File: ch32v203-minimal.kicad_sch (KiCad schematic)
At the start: 21 parts, among them J1 Conn_01x08, J3 Conn_01x04, J4 Conn_01x04, J5 Conn_02x10_Odd_Even, SW1 SW_Push, SW2 SW_Push, U1 AMS1117-3.3, U2 CH32V203K8T6, Y1 8MHz

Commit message: Rework layout
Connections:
- net NRST: now reaches C9.1, SW2.2, U2.4 (NRST)
- net BOOT0: now reaches R1.1, SW1.2, U2.31 (BOOT0/PB8)
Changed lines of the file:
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@@
+		)
+	)
+	(label "NRST"
+		(at 92.71 88.9 0)
+		(effects
+			(font
+				(size 1.27 1.27)
+			)
+			(justify left bottom)
 		)
 	)
@@
 		(effects
 			(font
+				(size 1.27 1.27)
+			)
+			(justify left bottom)
+		)
+	)
+	(label "BOOT0"
+		(at 210.82 78.74 0)
+		(effects
+			(font

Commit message: Add +5V connector
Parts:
- added J2: Conn_01x02_Pin, Connector_PinHeader_2.54mm:PinHeader_1x02_P2.54mm_Vertical, symbol Connector:Conn_01x02_Pin
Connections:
- net +5V: now also J2.1 (Pin_1)
- net GND: now also J2.2 (Pin_2)
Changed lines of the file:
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@@
 	)
 	(junction
+		(at 59.69 49.53)
+		(diameter 0)
+		(color 0 0 0 0)
+	)
+	(junction
 		(at 168.91 35.56)
 		(diameter 0)
@@
 	(wire
 		(pts
+			(xy 59.69 49.53) (xy 59.69 90.17)
+		)
+		(stroke
+			(width 0)
+			(type default)
+		)
+	)
+	(wire
+		(pts
 			(xy 88.9 76.2) (xy 93.98 76.2)
 		)
@@
 	(wire
 		(pts
-			(xy 59.69 25.4) (xy 59.69 90.17)
+			(xy 59.69 25.4) (xy 59.69 49.53)
 		)
 		(stroke
@@
 	(wire
 		(pts
+			(xy 52.07 49.53) (xy 59.69 49.53)
+		)
+		(stroke
+			(width 0)
+			(type default)
+		)
+	)
+	(wire
+		(pts
 			(xy 219.71 93.98) (xy 219.71 96.52)
 		)
@@
 	(wire
 		(pts
+			(xy 52.07 54.61) (xy 52.07 52.07)
+		)
+		(stroke
+			(width 0)
+			(type default)
+		)
+	)
+	(wire
+		(pts
 			(xy 182.88 39.37) (xy 195.58 39.37)
 		)
@@
 	)
 	(symbol
+		(lib_id "power:GND")
+		(at 52.07 54.61 0)
+		(mirror y)
+		(unit 1)
+		(body_style 1)
+		(exclude_from_sim no)
+		(in_bom yes)
+		(on_board yes)
+		(in_pos_files yes)
+		(dnp no)
+		(fields_autoplaced yes)
+		(property "Reference" "#PWR023"
+			(at 52.07 60.96 0)
+			(hide yes)
+			(show_name no)
+			(do_not_autoplace no)
+			(effects
+				(font
+					(size 1.27 1.27)
+				)
+			)
+		)
+		(property "Value" "GND"
+			(at 52.07 59.69 0)
+			(show_name no)
+			(do_not_autoplace no)
+			(effects
+				(font
+					(size 1.27 1.27)
+				)
+			)
+		)
+		(property "Footprint" ""
+			(at 52.07 54.61 0)
+			(hide yes)
+			(show_name no)
+			(do_not_autoplace no)
+			(effects
+				(font
+					(size 1.27 1.27)
+				)
+			)
+		)
+		(property "Datasheet" ""
+			(at 52.07 54.61 0)
+			(hide yes)
+			(show_name no)
+			(do_not_autoplace no)
+			(effects
+				(font
+					(size 1.27 1.27)
+				)
+			)
+		)
+		(property "Description" "Power symbol creates a global label with name \"GND\" , ground"
+			(at 52.07 54.61 0)
+			(hide yes)
+			(show_name no)
+			(do_not_autoplace no)
+			(effects
+				(font
+					(size 1.27 1.27)
+				)
+			)
+		)
+		(pin "1"
+		)
+		(instances
+			(project "ch32v203-minimal"
+				(path "/c4c3c12b-dd2c-4da1-bb89-311f762bf82a"
+					(reference "#PWR023")
+					(unit 1)
+				)
+			)
+		)
+	)
+	(symbol
 		(lib_id "Device:C")
 		(at 153.67 44.45 0)
@@
 					(unit 1)
 				)
+			)
+		)
+	)
+	(symbol
+		(lib_id "Connector:Conn_01x02_Pin")
+		(at 46.99 49.53 0)
+		(unit 1)
+		(body_style 1)
+		(exclude_from_sim no)
+		(in_bom yes)
+		(on_board yes)
+		(in_pos_files yes)
+		(dnp no)
+		(fields_autoplaced yes)
+		(property "Reference" "J2"
+			(at 47.625 44.45 0)
+			(show_name no)
+			(do_not_autoplace no)
+			(effects
+				(font
+					(size 1.27 1.27)
+				)
+			)
+		)
+		(property "Value" "Conn_01x02_Pin"
+			(at 47.625 46.99 0)
+			(show_name no)
+			(do_not_autoplace no)
+			(effects
+				(font
+					(size 1.27 1.27)
+				)
+			)
+		)
+		(property "Footprint" "Connector_PinHeader_2.54mm:PinHeader_1x02_P2.54mm_Vertical"
+			(at 46.99 49.53 0)
+			(hide yes)
+			(show_name no)
+			(do_not_autoplace no)
+			(effects
+				(font
+					(size 1.27 1.27)
+				)
+			)
+		)
+		(property "Datasheet" ""
+			(at 46.99 49.53 0)
+			(hide yes)
+			(show_name no)
+			(do_not_autoplace no)
+			(effects
+				(font
+					(size 1.27 1.27)
+				)
+			)
+		)
+		(property "Description" "Generic connector, single row, 01x02, script generated"
+			(at 46.99 49.53 0)
+			(hide yes)
+			(show_name no)
+			(do_not_autoplace no)
+			(effects
+				(font
+					(size 1.27 1.27)
+				)
+			)
+		)
+		(pin "1"
+		)
+		(pin "2"
+		)
+		(instances
+			(project "ch32v203-minimal"
+				(path "/c4c3c12b-dd2c-4da1-bb89-311f762bf82a"
+					(reference "J2")
+					(unit 1)
+				)

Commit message: Add proto board
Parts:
- added D2: SS14, Diode_SMD:D_SMA, symbol Diode:SS14
- added H1, H2, H3, H4, H5: MountingHole_Pad, MountingHole:MountingHole_2.2mm_M2_DIN965_Pad, symbol Mechanical:MountingHole_Pad
- added TP1, TP2: TestPoint, 0_Local:Proto-1x16, symbol Connector:TestPoint
- added TP10, TP11, TP12, TP13, TP14, TP15, TP16, TP17, TP18, TP3, TP4, TP5, TP6, TP7, TP8, TP9: TestPoint, 0_Local:Proto-1x4, symbol Connector:TestPoint
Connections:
- net +3V3: now also TP2.1
- net +5V: now also D2.2 (A); no longer C1.1, J2.1 (Pin_1), U1.3 (VI)
- net GND: now also H1.1, H2.1, H3.1, H4.1, H5.1, TP1.1
- new net Row 1: TP3.1
- new net Row 10: TP12.1
- new net Row 11: TP13.1
- new net Row 12: TP14.1
- new net Row 13: TP15.1
- new net Row 14: TP16.1
- new net Row 15: TP17.1
- new net Row 16: TP18.1
- new net Row 2: TP4.1
- new net Row 3: TP5.1
- new net Row 4: TP6.1
- new net Row 5: TP7.1
- new net Row 6: TP8.1
- new net Row 7: TP9.1
- new net Row 8: TP10.1
- new net Row 9: TP11.1
- new net VBUS: C1.1, D2.1 (K), J2.1 (Pin_1), U1.3 (VI)
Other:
- note added: "Proto Area"
- moved on the sheet: C1, C2, C3, C4, C5, C6, C7, C8, C9, D1, J1, J2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

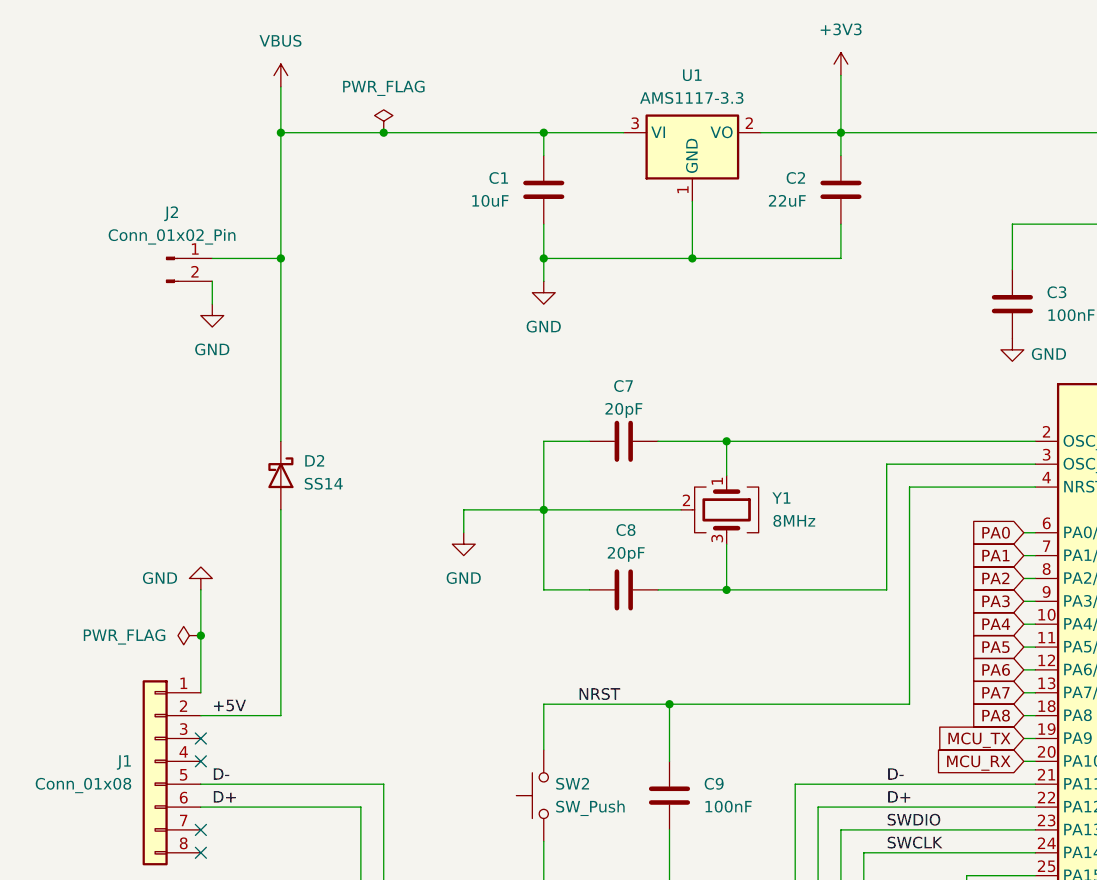
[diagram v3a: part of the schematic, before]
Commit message: Swap LDO for MCP1700
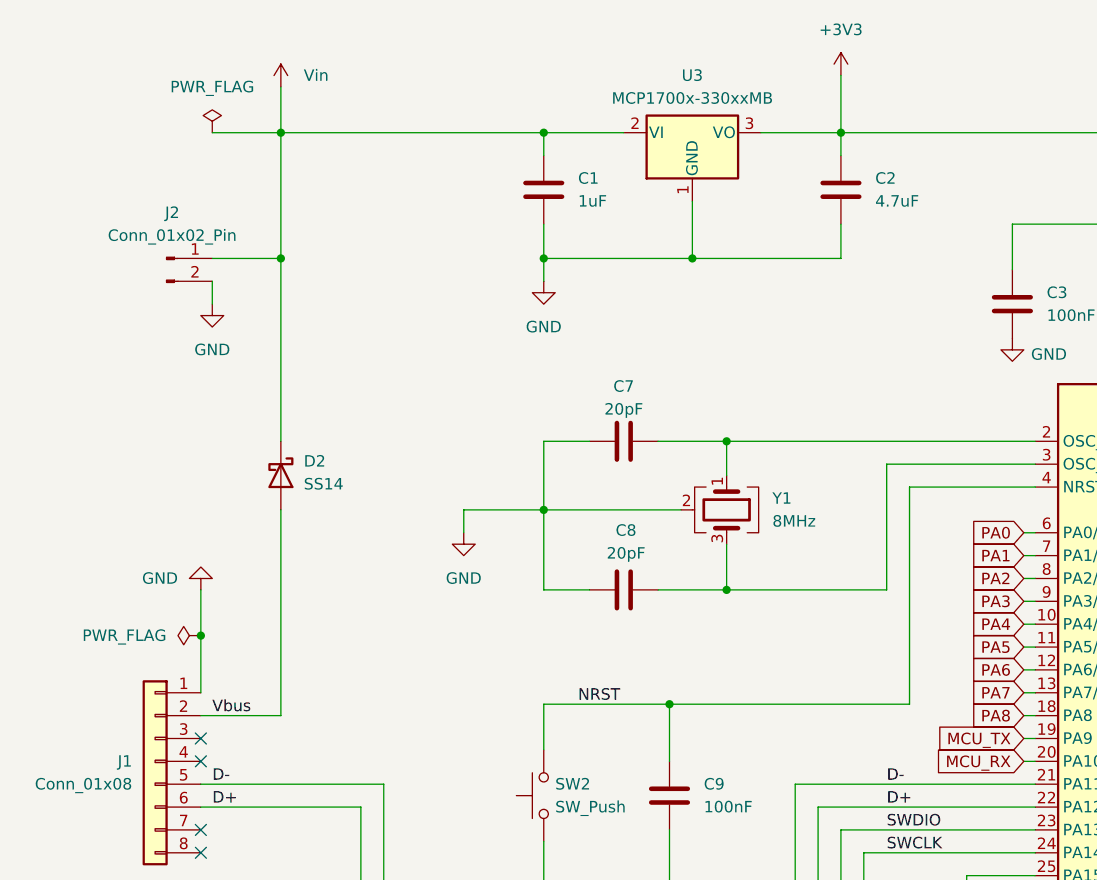
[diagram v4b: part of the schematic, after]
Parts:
- removed U1: AMS1117-3.3, Package_TO_SOT_SMD:SOT-223-3_TabPin2, symbol Regulator_Linear:AMS1117-3.3
- added U3: MCP1700x-330xxMB, Package_TO_SOT_SMD:SOT-89-3, symbol Regulator_Linear:MCP1700x-330xxMB
- C1: value 10uF -> 1uF; LCSC C9807 -> C1848
- C2: value 22uF -> 4.7uF; LCSC C5448976 -> C29823
- C3, C4, C5, C9: LCSC C110255 -> C24497
- C6: LCSC C377070 -> C1848
- R1: LCSC C2907370 -> C17902
- R2: LCSC C2907329 -> C2930375
- Y1: LCSC C400090 -> C2242
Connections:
- net +3V3: now also U3.3 (VO)
- net GND: now also U3.1 (GND)
- net +5V renamed Vbus
- net VBUS renamed Vin
- net Vin: now also U3.2 (VI)

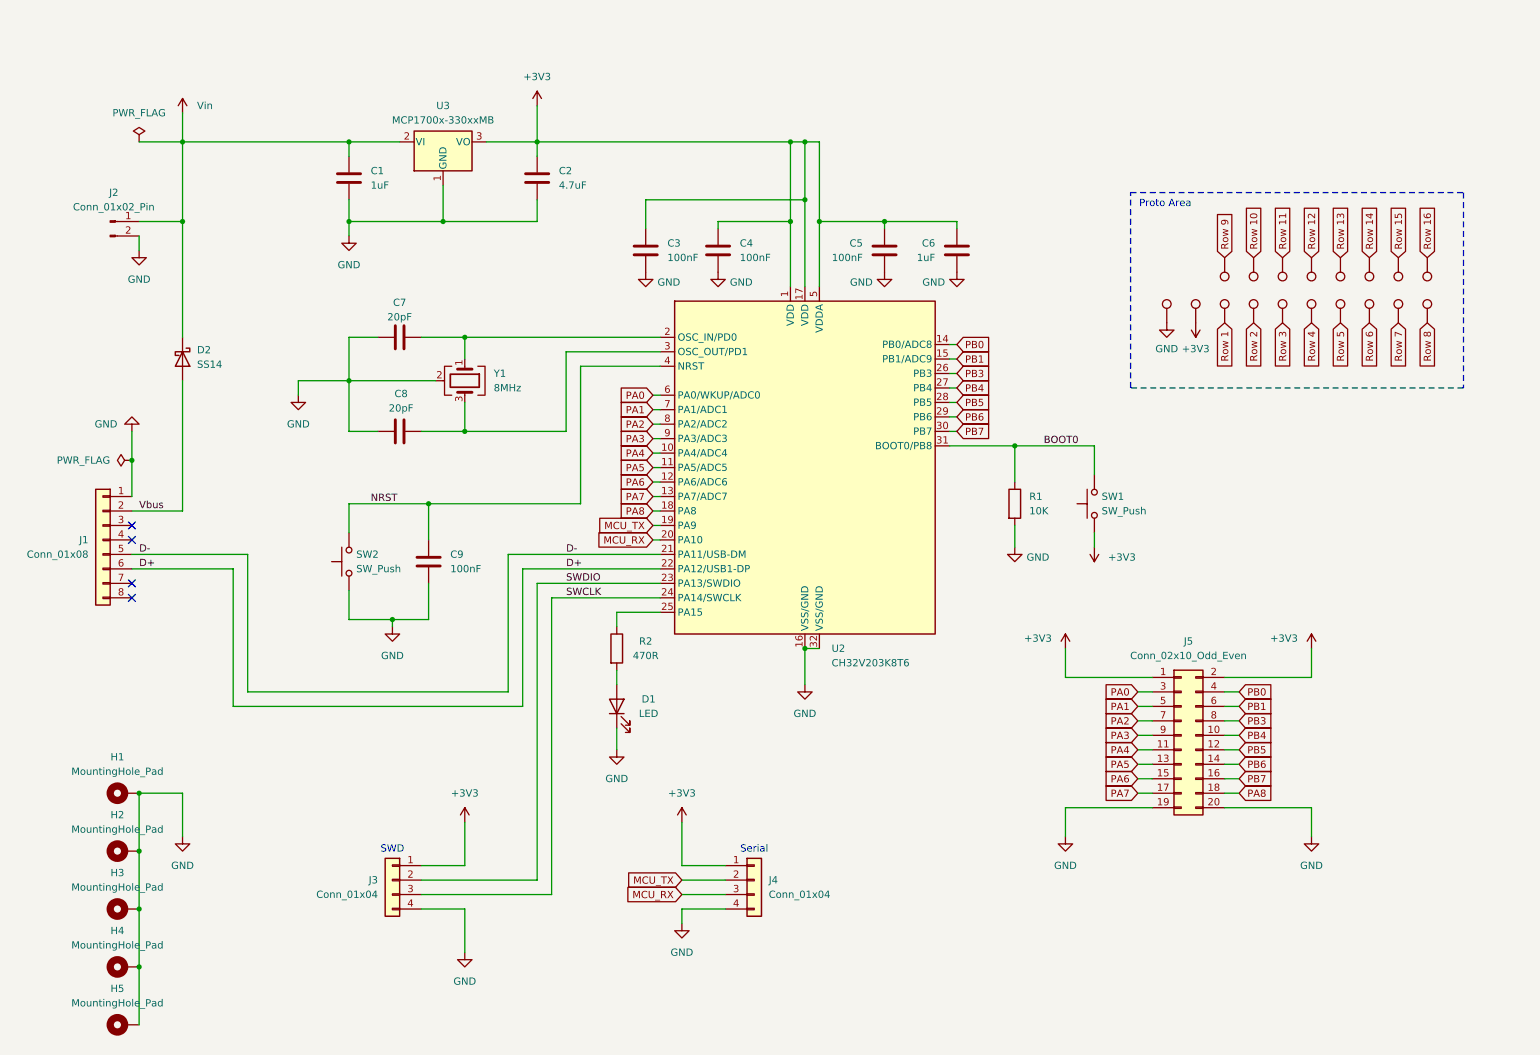
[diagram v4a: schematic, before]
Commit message: Add battery-charging circuit
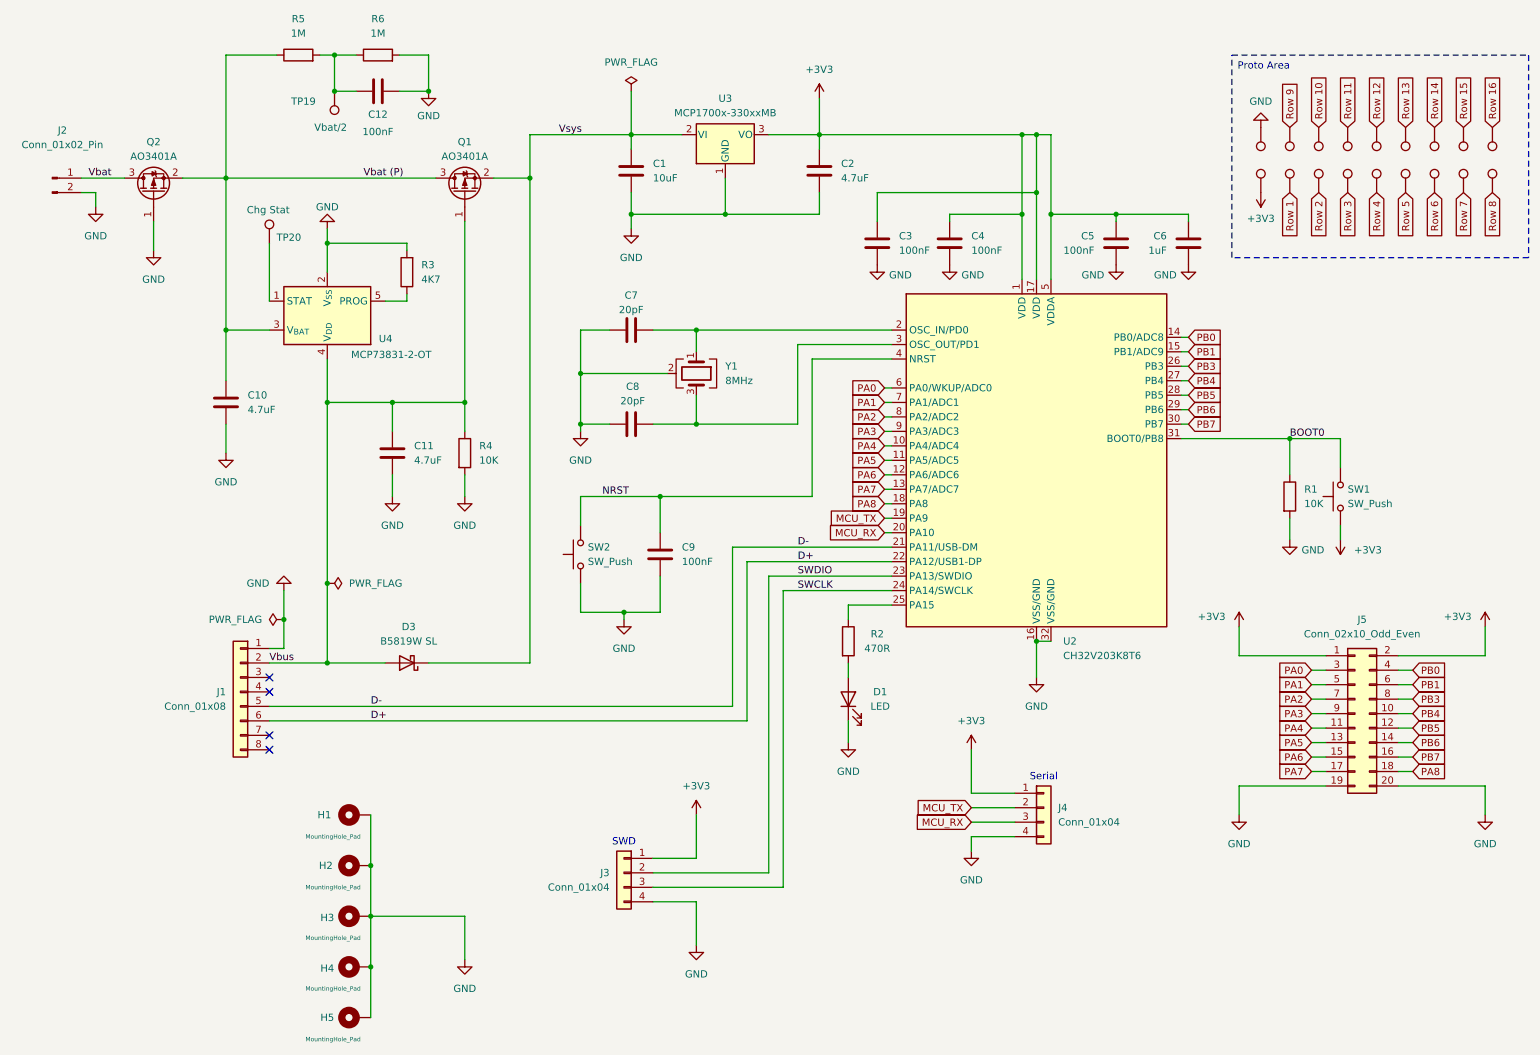
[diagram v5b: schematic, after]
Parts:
- removed D2: SS14, Diode_SMD:D_SMA, symbol Diode:SS14
- added C10, C11: 4.7uF, Capacitor_SMD:C_1206_3216Metric_Pad1.33x1.80mm_HandSolder, symbol Device:C
- added C12: 100nF, Capacitor_SMD:C_1206_3216Metric_Pad1.33x1.80mm_HandSolder, symbol Device:C
- added D3: B5819W SL, Diode_SMD:D_SOD-123, symbol Device:D_Schottky
- added Q1, Q2: AO3401A, Package_TO_SOT_SMD:SOT-23, symbol Transistor_FET:AO3401A
- added R3: 4K7, Resistor_SMD:R_1206_3216Metric_Pad1.30x1.75mm_HandSolder, symbol Device:R
- added R4: 10K, Resistor_SMD:R_1206_3216Metric_Pad1.30x1.75mm_HandSolder, symbol Device:R
- added R5, R6: 1M, Resistor_SMD:R_1206_3216Metric_Pad1.30x1.75mm_HandSolder, symbol Device:R
- added TP19: Vbat/2, 0_Local:TP-PlatedHole, symbol Connector:TestPoint
- added TP20: Chg Stat, 0_Local:TP-PlatedHole, symbol Connector:TestPoint
- added U4: MCP73831-2-OT, Package_TO_SOT_SMD:SOT-23-5, symbol Battery_Management:MCP73831-2-OT
- C1: value 1uF -> 10uF; LCSC C1848 -> C13585
- C7, C8: LCSC C107193 -> C377026
- D1: LCSC C965815 -> C3646937
- J2: footprint Connector_PinHeader_2.54mm:PinHeader_1x02_P2.54mm_Vertical -> Connector_JST:JST_PH_B2B-PH-K_1x02_P2.00mm_Vertical
- Y1: LCSC C2242 -> C400090
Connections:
- net GND: now also C10.2, C11.2, C12.2, Q2.1 (G), R3.2, R4.2, R6.2, U4.2 (V_{SS})
- net Vbus: now also C11.1, D3.2 (A), Q1.1 (G), R4.1, U4.4 (V_{DD})
- net Vin renamed Vsys
- net Vsys: now also D3.1 (K), Q1.2 (S); no longer J2.1 (Pin_1)
- new net: C12.1, R5.2, R6.1, TP19.1
- new net: R3.1, U4.5 (PROG)
- new net: TP20.1, U4.1 (STAT)
- new net Vbat: J2.1 (Pin_1), Q2.3 (D)
- new net Vbat (P): C10.1, Q1.3 (D), Q2.2 (S), R5.1, U4.3 (V_{BAT})
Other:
- moved on the sheet: C1, C2, C3, C4, C5, C6, C7, C8, C9, D1, H1, H2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
